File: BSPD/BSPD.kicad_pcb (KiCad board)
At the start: 2 copper layers, 65.1 x 52.9 mm, 59 parts, among them J2 Conn_01x04, J3 Conn_01x02, K2 G2RL-2, Q1 AO3401A, Q2 BSS138, Q3 BSS138, U2 AMS1117-5.0

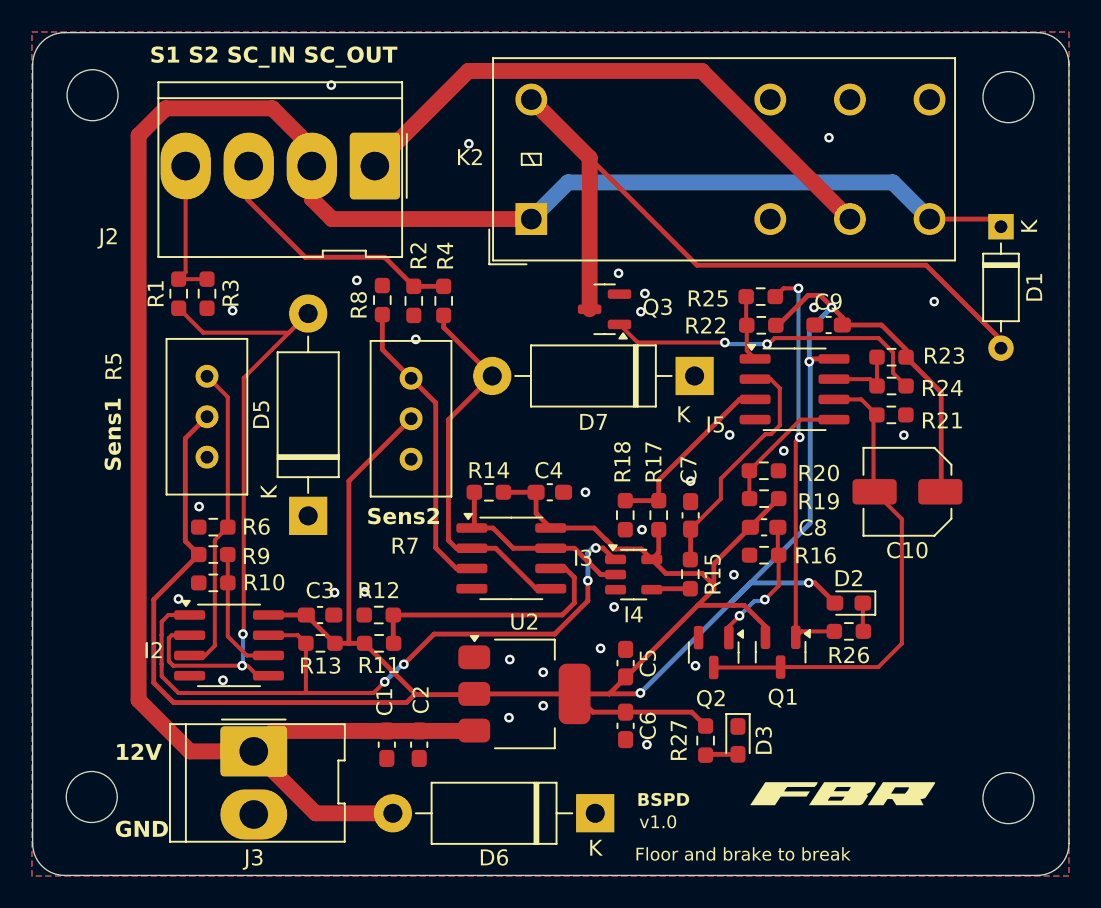
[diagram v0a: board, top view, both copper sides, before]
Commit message: Increase width of SDC track
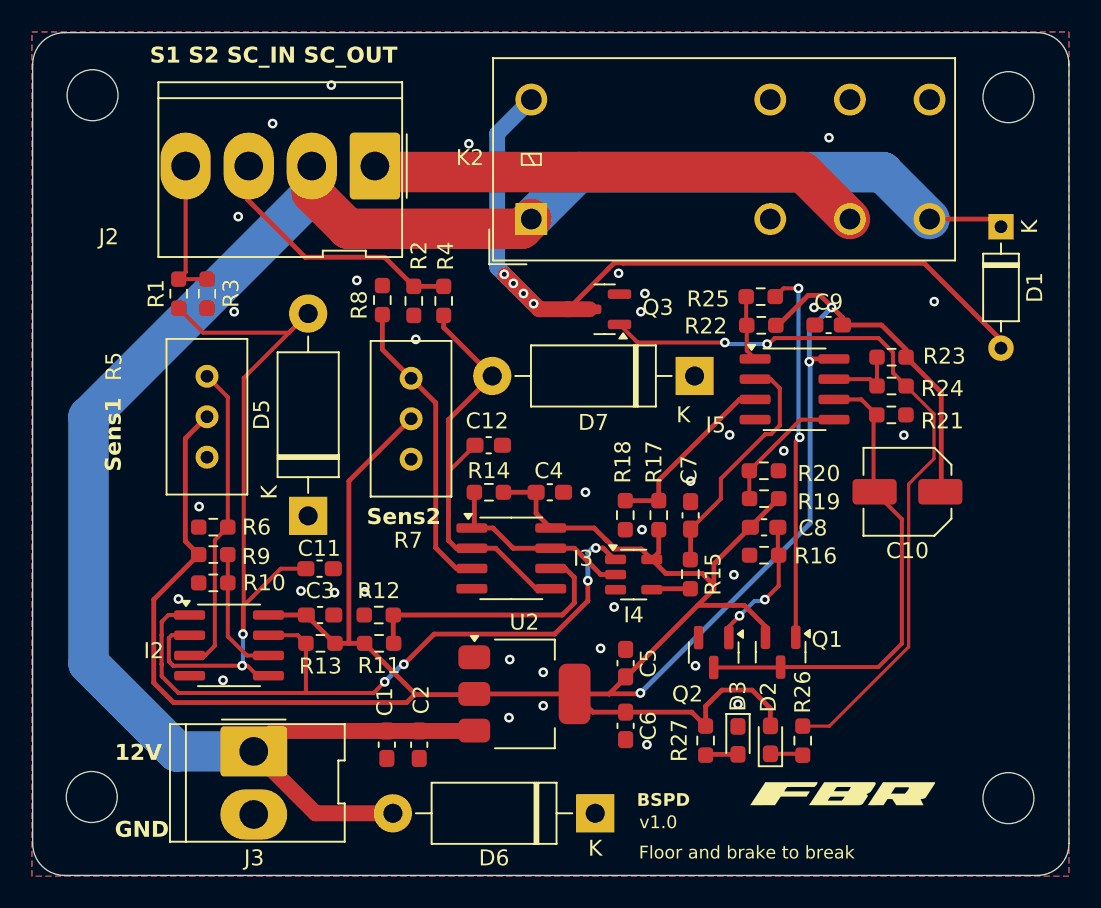
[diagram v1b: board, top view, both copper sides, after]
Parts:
- added C11: 100n, Capacitor_SMD:C_0603_1608Metric_Pad1.08x0.95mm_HandSolder, F.Cu at (105.8, 87.9)
- added C12: 100n, Capacitor_SMD:C_0603_1608Metric_Pad1.08x0.95mm_HandSolder, F.Cu at (116.4, 80.1)
- R26: value 330 -> 470
- R27: value 470 -> 560
- moved D2 9.90 mm to (134.1, 98.6), turned to 90 degrees
- moved R26 7.44 mm to (136.1, 98.7), turned to -90 degrees
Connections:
- R26 pad 1: Net-(Q1-G) -> Net-(Q3-G)
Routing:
- net Net-(Q3-G): track 20.7 -> 47.1 mm
- net +12V: track 131.7 -> 124.5 mm
- net Net-(D1-A): track 45.7 -> 51.2 mm, vias 0 -> 4
- net /SDC_OUT: track 36.2 -> 31.2 mm
- net Net-(D5-A2): track 43.2 -> 48.1 mm
- net Net-(D7-A2): track 25.0 -> 29.3 mm
- net Net-(Q1-G): track 26.3 -> 23.7 mm
- net +5V: track 185.6 -> 185.1 mm, vias 4 -> 3
- net GND: vias 31 -> 35
